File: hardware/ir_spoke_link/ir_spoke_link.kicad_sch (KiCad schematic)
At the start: 14 parts, among them J1 XIAO_LEFT: D0,D1,D2,D3,D4,D5,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, J2 XIAO_RIGHT: D10,D9,D8,D7,3V3,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, Q1 S8050, U1 TSOP57438TT1 38kHz

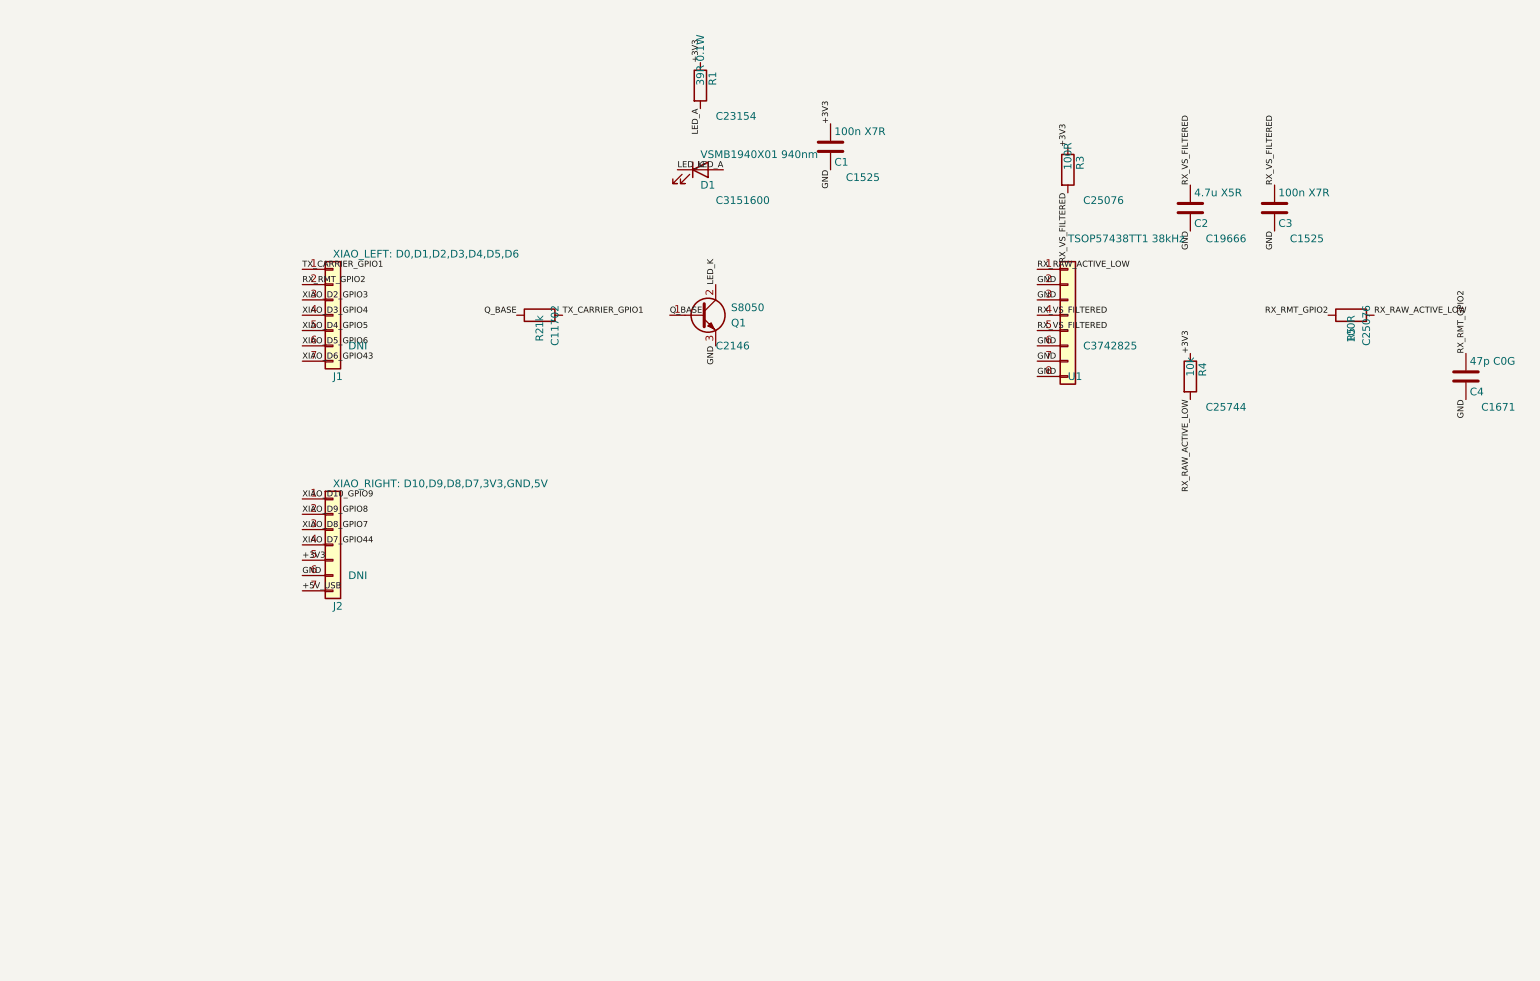
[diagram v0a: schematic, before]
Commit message: Build discrete IR spoke sensor system and technical docs
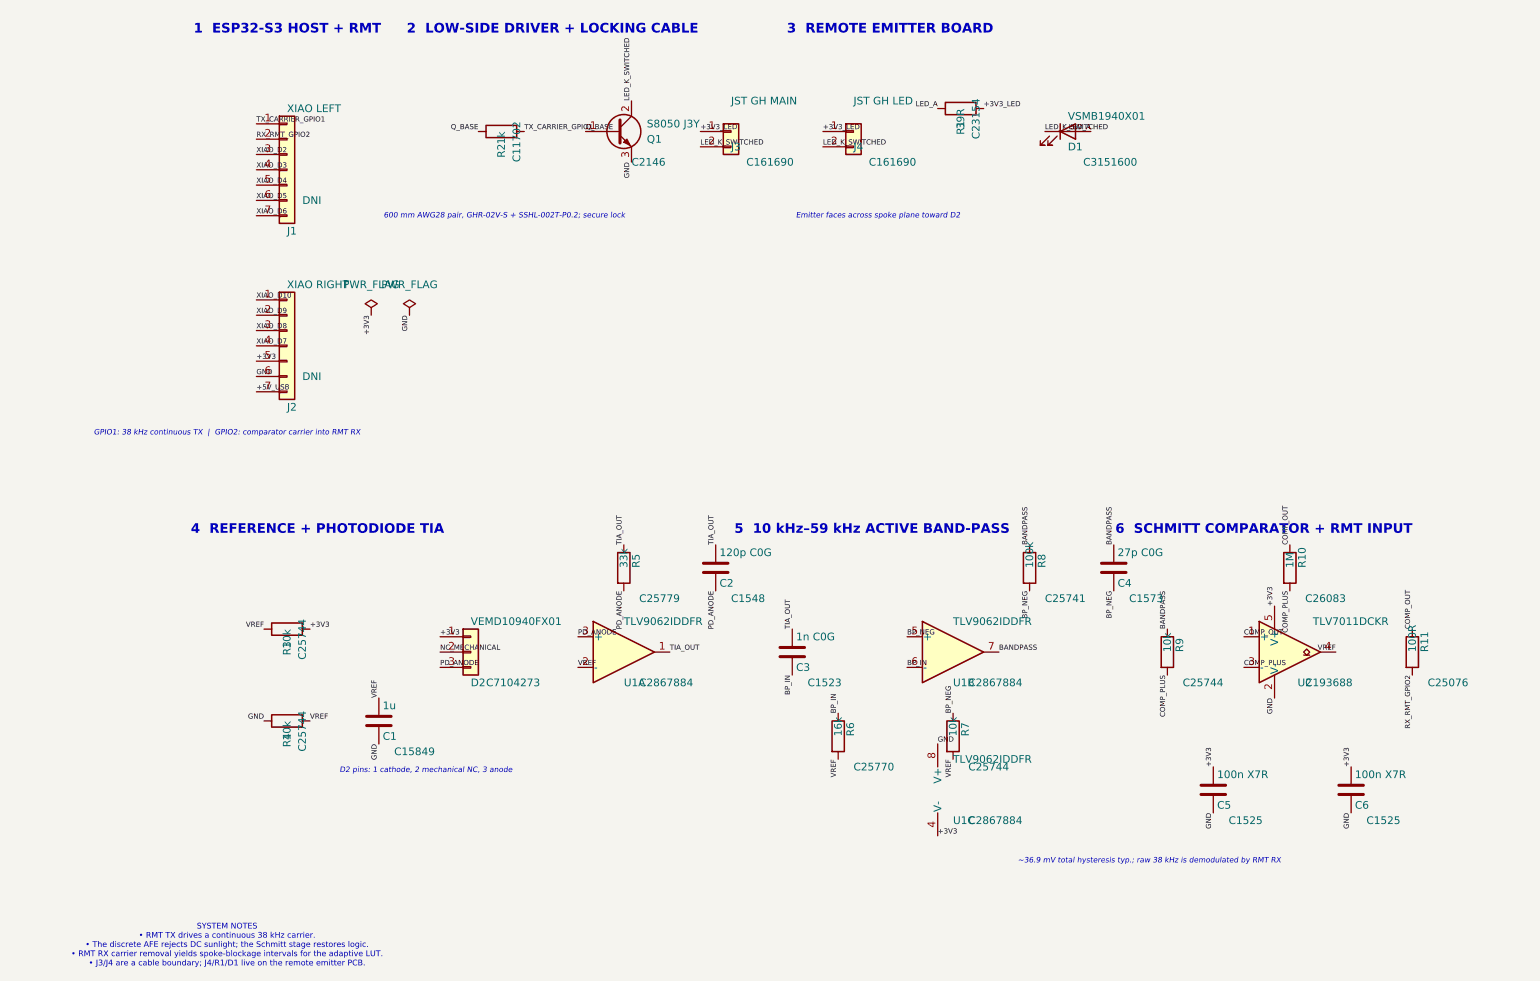
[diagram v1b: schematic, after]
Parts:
- removed U1: TSOP57438TT1 38kHz, IR_Spoke_Link:TSOP57_Belobog_4x4mm, symbol Connector_Generic:Conn_01x08
- added C5, C6: 100n X7R, Capacitor_SMD:C_0402_1005Metric, symbol Device:C
- added D2: VEMD10940FX01, IR_Spoke_Link:VEMD10940F_SideView, symbol Connector_Generic:Conn_01x03
- added J3: JST GH MAIN, Connector_JST:JST_GH_BM02B-GHS-TBT_1x02-1MP_P1.25mm_Vertical, symbol Connector_Generic:Conn_01x02
- added J4: JST GH LED, Connector_JST:JST_GH_BM02B-GHS-TBT_1x02-1MP_P1.25mm_Vertical, symbol Connector_Generic:Conn_01x02
- added R10: 1M, Resistor_SMD:R_0402_1005Metric, symbol Device:R
- added R11: 100R, Resistor_SMD:R_0402_1005Metric, symbol Device:R
- added R6: 16k, Resistor_SMD:R_0402_1005Metric, symbol Device:R
- added R7, R9: 10k, Resistor_SMD:R_0402_1005Metric, symbol Device:R
- added R8: 100k, Resistor_SMD:R_0402_1005Metric, symbol Device:R
- added U1: TLV9062IDDFR, Package_TO_SOT_SMD:SOT-23-8, symbol Amplifier_Operational:TLV9062
- added U2: TLV7011DCKR, Package_TO_SOT_SMD:SOT-353_SC-70-5, symbol Comparator:LMV331
- C1: value 100n X7R -> 1u; footprint Capacitor_SMD:C_0402_1005Metric -> Capacitor_SMD:C_0603_1608Metric; LCSC C1525 -> C15849
- C2: value 4.7u X5R -> 120p C0G; footprint Capacitor_SMD:C_0603_1608Metric -> Capacitor_SMD:C_0402_1005Metric; LCSC C19666 -> C1548
- C3: value 100n X7R -> 1n C0G; LCSC C1525 -> C1523
- C4: value 47p C0G -> 27p C0G; LCSC C1671 -> C1573
- D1: value VSMB1940X01 940nm -> VSMB1940X01
- J1: value XIAO_LEFT: D0,D1,D2,D3,D4,D5,D6 -> XIAO LEFT
- J2: value XIAO_RIGHT: D10,D9,D8,D7,3V3,GND,5V -> XIAO RIGHT
- Q1: value S8050 -> S8050 J3Y
- R1: value 39R 0.1W -> 39R
- R3: value 100R -> 10k; LCSC C25076 -> C25744
- R5: value 100R -> 33k; LCSC C25076 -> C25779
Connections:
- net +3V3: now also R3.2, C5.1, C6.1, D2.1 (Pin_1), U1.4 (V-), U2.5 (V+); no longer C1.1, R1.1, R3.1, R4.1
- net GND: now also R4.1, C5.2, C6.2, U1.8 (V+), U2.2 (V-); no longer C2.2, C3.2, C4.2
- net LED_A: now also R1.1; no longer R1.2
- net RX_RMT_GPIO2: now also R11.2; no longer C4.1, R5.1
- net LED_K renamed LED_K_SWITCHED
- net LED_K_SWITCHED: now also J3.2 (Pin_2), J4.2 (Pin_2)
- net RX_RAW_ACTIVE_LOW renamed PD_ANODE
- net PD_ANODE: now also C2.2, D2.3 (Pin_3), U1.3 (+); no longer R4.2
- net RX_VS_FILTERED renamed TIA_OUT
- net TIA_OUT: now also R5.1, U1.1; no longer R3.2
- net XIAO_D10_GPIO9 renamed XIAO_D10
- net XIAO_D2_GPIO3 renamed XIAO_D2
- net XIAO_D3_GPIO4 renamed XIAO_D3
- net XIAO_D4_GPIO5 renamed XIAO_D4
- net XIAO_D5_GPIO6 renamed XIAO_D5
- net XIAO_D6_GPIO43 renamed XIAO_D6
- net XIAO_D7_GPIO44 renamed XIAO_D7
- net XIAO_D8_GPIO7 renamed XIAO_D8
- net XIAO_D9_GPIO8 renamed XIAO_D9
- new net +3V3_LED: J3.1 (Pin_1), J4.1 (Pin_1), R1.2
- new net BANDPASS: C4.1, R8.1, R9.1, U1.7
- new net BP_IN: C3.2, R6.1, U1.6 (-)
- new net BP_NEG: C4.2, R7.1, R8.2, U1.5 (+)
- new net COMP_OUT: R10.1, R11.1, U2.1 (+)
- new net COMP_PLUS: R10.2, R9.2, U2.3 (-)
- new net NC_MECHANICAL: D2.2 (Pin_2)
- new net VREF: C1.1, R3.1, R4.2, R6.2, R7.2, U1.2 (-), U2.4
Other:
- note added: "1 ESP32-S3 HOST + RMT"
- note added: "2 LOW-SIDE DRIVER + LOCKING CABLE"
- note added: "3 REMOTE EMITTER BOARD"
- note added: "4 REFERENCE + PHOTODIODE TIA"
- note added: "5 10 kHz–59 kHz ACTIVE BAND-PASS"
- note added: "6 SCHMITT COMPARATOR + RMT INPUT"
- note added: "600 mm AWG28 pair, GHR-02V-S + SSHL-002T-P0.2; secure lock"
- note added: "D2 pins: 1 cathode, 2 mechanical NC, 3 anode"
- note added: "Emitter faces across spoke plane toward D2"
- note added: "GPIO1: 38 kHz continuous TX | GPIO2: comparator carrier into RMT RX"
- note added: "SYSTEM NOTES • RMT TX drives a continuous 38 kHz carrier. • The discrete AFE rejects DC sunlight; the Schmitt stage restores logic. • RMT RX carrier removal yields spoke-blockage intervals for the adaptive LUT. • J3/J4 are a cable boundary; J4/R1/D1 live on the remote emitter PCB."
- note added: "~36.9 mV total hysteresis typ.; raw 38 kHz is demodulated by RMT RX"
- title: IR Spoke Link -> IR Spoke Sensor

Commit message: Make IR carrier configurable and link full simulation stack
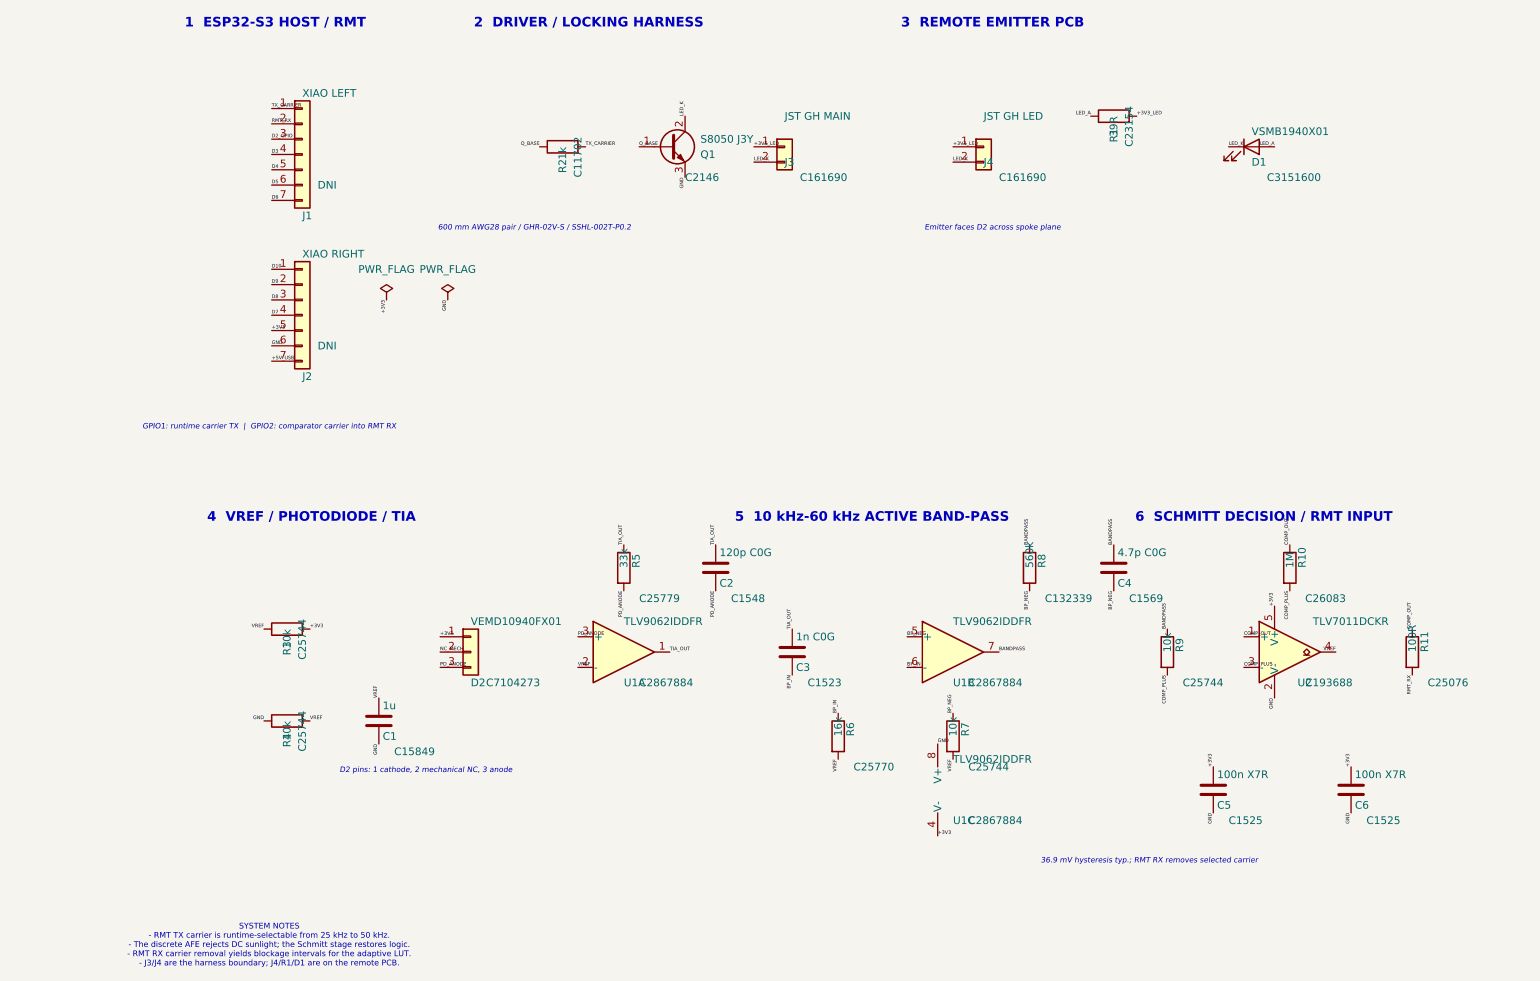
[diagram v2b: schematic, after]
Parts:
- C4: value 27p C0G -> 4.7p C0G; LCSC C1573 -> C1569
- R8: value 100k -> 560k; LCSC C25741 -> C132339
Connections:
- net LED_K_SWITCHED renamed LED_K
- net NC_MECHANICAL renamed NC_MECH
- net RX_RMT_GPIO2 renamed RMT_RX
- net TX_CARRIER_GPIO1 renamed TX_CARRIER
- net XIAO_D10 renamed D10
- net XIAO_D2 renamed D2_GPIO
- net XIAO_D3 renamed D3
- net XIAO_D4 renamed D4
- net XIAO_D5 renamed D5
- net XIAO_D6 renamed D6
- net XIAO_D7 renamed D7
- net XIAO_D8 renamed D8
- net XIAO_D9 renamed D9
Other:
- note added: "1 ESP32-S3 HOST / RMT"
- note added: "2 DRIVER / LOCKING HARNESS"
- note added: "3 REMOTE EMITTER PCB"
- note added: "36.9 mV hysteresis typ.; RMT RX removes selected carrier"
- note added: "4 VREF / PHOTODIODE / TIA"
- note added: "5 10 kHz-60 kHz ACTIVE BAND-PASS"
- note added: "6 SCHMITT DECISION / RMT INPUT"
- note added: "600 mm AWG28 pair / GHR-02V-S / SSHL-002T-P0.2"
- note added: "Emitter faces D2 across spoke plane"
- note added: "GPIO1: runtime carrier TX | GPIO2: comparator carrier into RMT RX"
- note added: "SYSTEM NOTES - RMT TX carrier is runtime-selectable from 25 kHz to 50 kHz. - The discrete AFE rejects DC sunlight; the Schmitt stage restores logic. - RMT RX carrier removal yields blockage intervals for the adaptive LUT. - J3/J4 are the harness boundary; J4/R1/D1 are on the remote PCB."
- note removed: "1 ESP32-S3 HOST + RMT"
- note removed: "2 LOW-SIDE DRIVER + LOCKING CABLE"
- note removed: "3 REMOTE EMITTER BOARD"
- note removed: "4 REFERENCE + PHOTODIODE TIA"
- note removed: "5 10 kHz–59 kHz ACTIVE BAND-PASS"
- note removed: "6 SCHMITT COMPARATOR + RMT INPUT"
- note removed: "600 mm AWG28 pair, GHR-02V-S + SSHL-002T-P0.2; secure lock"
- note removed: "Emitter faces across spoke plane toward D2"
- note removed: "GPIO1: 38 kHz continuous TX | GPIO2: comparator carrier into RMT RX"
- note removed: "SYSTEM NOTES • RMT TX drives a continuous 38 kHz carrier. • The discrete AFE rejects DC sunlight; the Schmitt stage restores logic. • RMT RX carrier removal yields spoke-blockage intervals for the adaptive LUT. • J3/J4 are a cable boundary; J4/R1/D1 live on the remote emitter PCB."
- note removed: "~36.9 mV total hysteresis typ.; raw 38 kHz is demodulated by RMT RX"
